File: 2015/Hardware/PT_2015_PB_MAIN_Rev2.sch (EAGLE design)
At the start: 135 parts, among them Q1 Q_ACS711LC, Q11 Q_IRFS7437PbF, Q12 2N7002, Q14 Q_IRFS7437PbF, Q16 Q_IRFS7437PbF, Q18 Q_FDT86102LZ, Q20 Q_IRFS7437PbF, Q4 Q_ACS711LC, Q5 Q_ACS711LC, Q6 Q_IRFS7437PbF, Q7 Q_IRFS7437PbF, Q9 Q_IRFS7437PbF

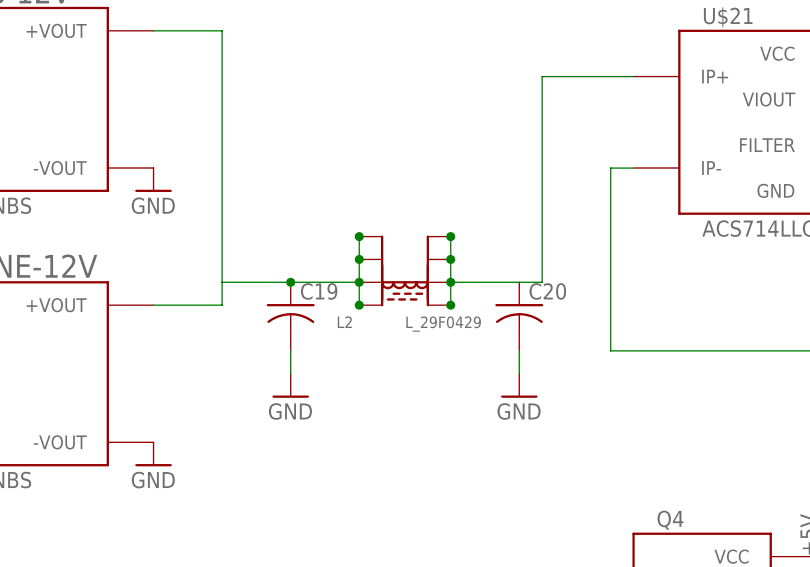
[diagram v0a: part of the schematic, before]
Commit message: Removed ferrite bede on 12V non-critical output
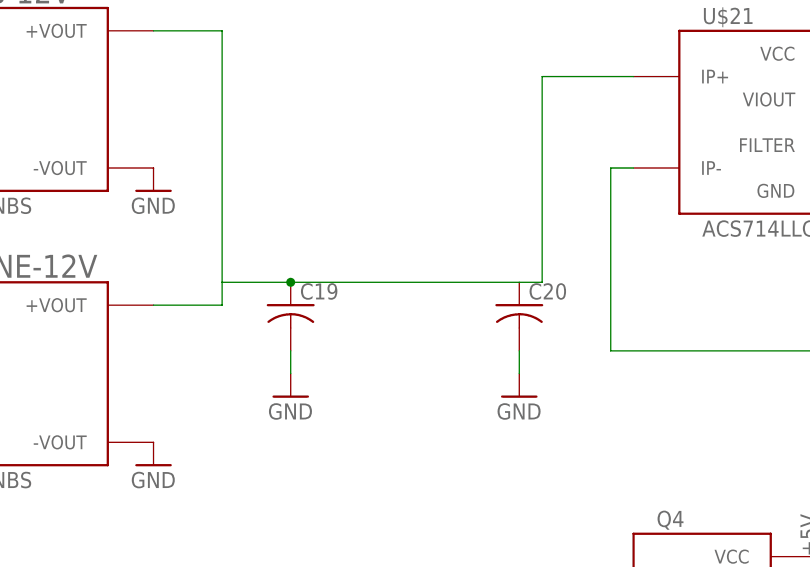
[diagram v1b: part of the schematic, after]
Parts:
- removed L2: L_29F0429, MRDT-2014-All:L_29F0429
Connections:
- removed net N$11: C20.1, L2.5, L2.6, L2.7, L2.8, U$21.IP+
- net N$7: now also C20.1, U$21.IP+; no longer L2.1, L2.2, L2.3, L2.4

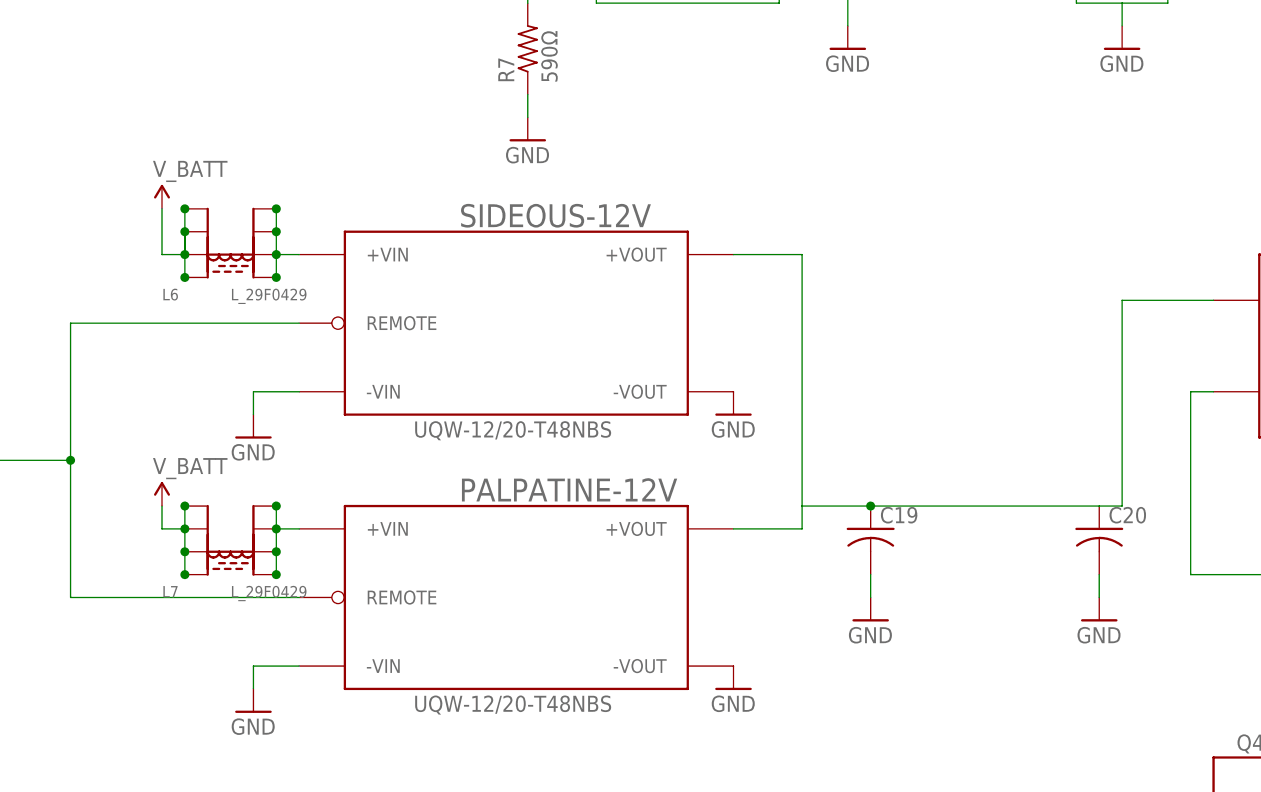
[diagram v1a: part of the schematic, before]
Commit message: Replaced input ferrites and output caps on 12V NC
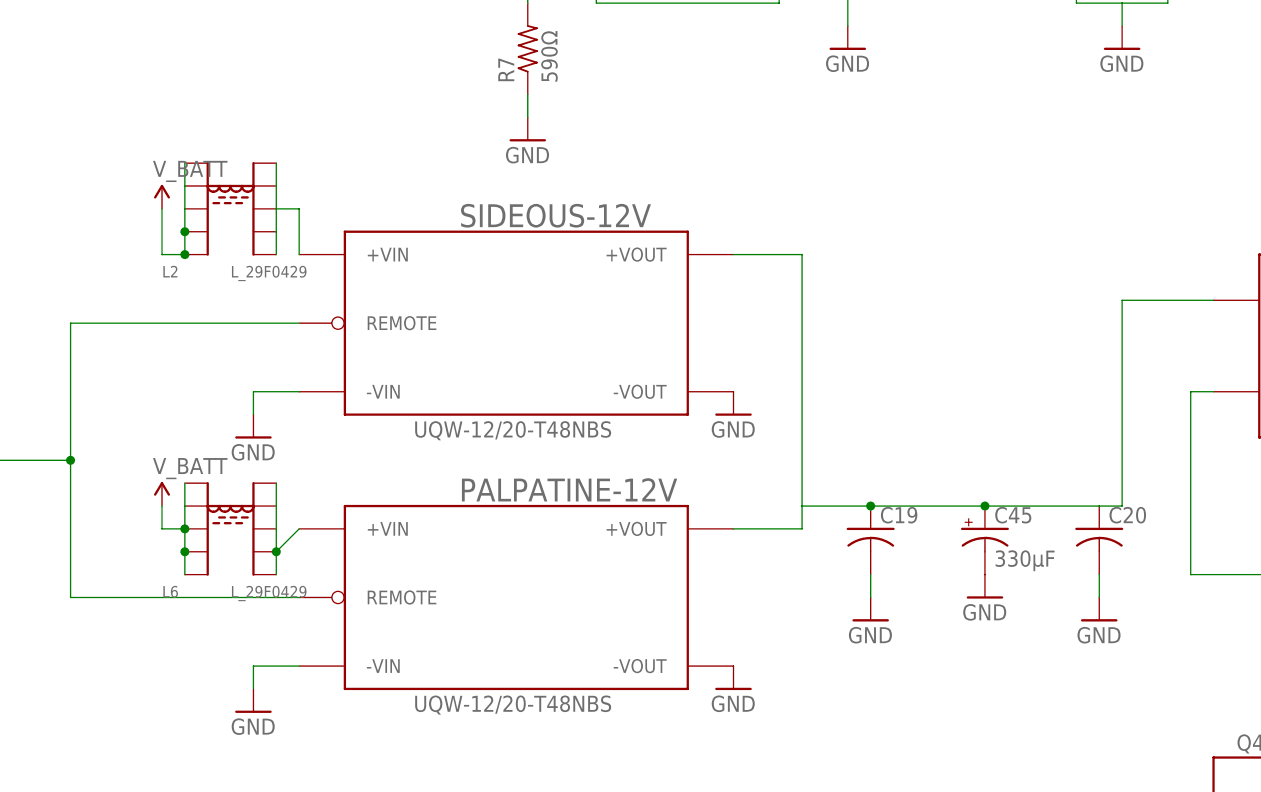
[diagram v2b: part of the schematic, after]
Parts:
- removed L7: L_29F0429, MRDT-2014-All:L_29F0429
- added C45: 330µF, resistor:CPOL-USE5-8.5
- added L2: L_29F0429, MRDT-2015-PowerBoard:L_29F0429
- L6: device MRDT-2014-All:L_29F0429 -> MRDT-2015-PowerBoard:L_29F0429
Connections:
- net GND: now also C45.-
- net N$5: now also L6.10, L6.6, L6.7, L6.8; no longer L7.5, L7.6, L7.7, L7.8
- net N$6: now also L2.10, L2.6, L2.7, L2.8, L2.9; no longer L6.5, L6.6, L6.7, L6.8
- net N$7: now also C45.+
- net V_BATT: now also L2.1, L2.2, L2.3, L2.4, L2.5, L6.5; no longer L7.1, L7.2, L7.3, L7.4
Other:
- moved on the sheet: L6
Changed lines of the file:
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@@
 <?xml version="1.0" encoding="utf-8"?>
 <!DOCTYPE eagle SYSTEM "eagle.dtd">
-<eagle version="7.0.0">
+<eagle version="6.5.0">
 <drawing>
 <settings>
@@
 <part name="L4" library="MRDT-2014-All" deviceset="L_29F0429" device=""/>
 <part name="L5" library="MRDT-2014-All" deviceset="L_29F0429" device=""/>
-<part name="L6" library="MRDT-2014-All" deviceset="L_29F0429" device=""/>
-<part name="L7" library="MRDT-2014-All" deviceset="L_29F0429" device=""/>
 <part name="L8" library="MRDT-2014-All" deviceset="L_29F0429" device=""/>
 <part name="U$2" library="MRDT-2014-All" deviceset="D_SD12T1G" device=""/>
@@
 <part name="GND89" library="SparkFun-Aesthetics" deviceset="GND" device=""/>
 <part name="ARM_P" library="MRDT-2015-PowerBoard" deviceset="H_WR-TBL_32*1*0002" device="HORIZ"/>
+<part name="C45" library="resistor" deviceset="CPOL-US" device="E5-8.5" value="330µF"/>
+<part name="GND90" library="SparkFun-Aesthetics" deviceset="GND" device=""/>
+<part name="L2" library="MRDT-2015-PowerBoard" deviceset="L_29F0429" device=""/>
+<part name="L6" library="MRDT-2015-PowerBoard" deviceset="L_29F0429" device=""/>
 </parts>
 <sheets>
@@
 <instance part="L4" gate="G$1" x="106.68" y="0"/>
 <instance part="L5" gate="G$1" x="25.4" y="119.38"/>
-<instance part="L6" gate="G$1" x="33.02" y="81.28"/>
-<instance part="L7" gate="G$1" x="33.02" y="48.26"/>
 <instance part="L8" gate="G$1" x="25.4" y="-2.54"/>
 <instance part="U$2" gate="G$1" x="129.54" y="-5.08" rot="R90"/>
@@
 <instance part="GND89" gate="1" x="-474.98" y="200.66"/>
 <instance part="ARM_P" gate="G$1" x="-528.32" y="144.78"/>
+<instance part="C45" gate="G$1" x="116.84" y="50.8"/>
+<instance part="GND90" gate="1" x="116.84" y="43.18"/>
+<instance part="L2" gate="G$1" x="33.02" y="83.82"/>
+<instance part="L6" gate="G$1" x="33.02" y="48.26"/>
 </instances>
 <busses>
@@
 <pinref part="C44" gate="G$1" pin="2"/>
 <pinref part="GND89" gate="1" pin="GND"/>
+</segment>
+<segment>
+<pinref part="C45" gate="G$1" pin="-"/>
+<pinref part="GND90" gate="1" pin="GND"/>
 </segment>
 </net>
@@
 <pinref part="SUPPLY3" gate="G$1" pin="V_BATT"/>
 <wire x1="25.4" y1="81.28" x2="25.4" y2="86.36" width="0.1524" layer="91"/>
-<pinref part="L6" gate="G$1" pin="1"/>
 <wire x1="25.4" y1="81.28" x2="27.94" y2="81.28" width="0.1524" layer="91"/>
-<pinref part="L6" gate="G$1" pin="2"/>
-<wire x1="27.94" y1="78.74" x2="27.94" y2="81.28" width="0.1524" layer="91"/>
-<pinref part="L6" gate="G$1" pin="3"/>
-<wire x1="27.94" y1="83.82" x2="27.94" y2="81.28" width="0.1524" layer="91"/>
-<pinref part="L6" gate="G$1" pin="4"/>
+<junction x="27.94" y="81.28"/>
 <wire x1="27.94" y1="81.28" x2="27.94" y2="83.82" width="0.1524" layer="91"/>
-<junction x="27.94" y="78.74"/>
-<junction x="27.94" y="81.28"/>
+<pinref part="L2" gate="G$1" pin="3"/>
+<pinref part="L2" gate="G$1" pin="2"/>
+<wire x1="27.94" y1="83.82" x2="27.94" y2="86.36" width="0.1524" layer="91"/>
 <junction x="27.94" y="83.82"/>
-<wire x1="27.94" y1="83.82" x2="27.94" y2="86.36" width="0.1524" layer="91"/>
-<junction x="27.94" y="86.36"/>
+<pinref part="L2" gate="G$1" pin="1"/>
+<pinref part="L2" gate="G$1" pin="4"/>
+<wire x1="27.94" y1="88.9" x2="27.94" y2="86.36" width="0.1524" layer="91"/>
+<pinref part="L2" gate="G$1" pin="5"/>
+<wire x1="27.94" y1="91.44" x2="27.94" y2="88.9" width="0.1524" layer="91"/>
 </segment>
 <segment>
 <pinref part="SUPPLY4" gate="G$1" pin="V_BATT"/>
 <wire x1="25.4" y1="50.8" x2="25.4" y2="53.34" width="0.1524" layer="91"/>
-<pinref part="L7" gate="G$1" pin="3"/>
 <wire x1="25.4" y1="50.8" x2="27.94" y2="50.8" width="0.1524" layer="91"/>
-<pinref part="L7" gate="G$1" pin="4"/>
 <wire x1="27.94" y1="50.8" x2="27.94" y2="53.34" width="0.1524" layer="91"/>
-<pinref part="L7" gate="G$1" pin="2"/>
+<wire x1="27.94" y1="45.72" x2="27.94" y2="48.26" width="0.1524" layer="91"/>
+<junction x="27.94" y="50.8"/>
+<pinref part="L6" gate="G$1" pin="4"/>
+<pinref part="L6" gate="G$1" pin="3"/>
+<pinref part="L6" gate="G$1" pin="2"/>
 <wire x1="27.94" y1="48.26" x2="27.94" y2="50.8" width="0.1524" layer="91"/>
-<pinref part="L7" gate="G$1" pin="1"/>
-<wire x1="27.94" y1="45.72" x2="27.94" y2="48.26" width="0.1524" layer="91"/>
-<junction x="27.94" y="53.34"/>
-<junction x="27.94" y="50.8"/>
 <junction x="27.94" y="48.26"/>
-<junction x="27.94" y="45.72"/>
+<pinref part="L6" gate="G$1" pin="1"/>
+<pinref part="L6" gate="G$1" pin="5"/>
+<wire x1="27.94" y1="55.88" x2="27.94" y2="53.34" width="0.1524" layer="91"/>
 </segment>
 <segment>
@@
 <net name="N$5" class="0">
 <segment>
-<pinref part="L7" gate="G$1" pin="8"/>
-<pinref part="L7" gate="G$1" pin="5"/>
-<wire x1="38.1" y1="53.34" x2="38.1" y2="50.8" width="0.1524" layer="91"/>
+<wire x1="38.1" y1="50.8" x2="38.1" y2="48.26" width="0.1524" layer="91"/>
 <pinref part="PALPATINE-12V" gate="G$1" pin="+VIN"/>
-<wire x1="38.1" y1="50.8" x2="38.1" y2="48.26" width="0.1524" layer="91"/>
 <wire x1="38.1" y1="48.26" x2="38.1" y2="45.72" width="0.1524" layer="91"/>
-<junction x="38.1" y="45.72"/>
-<pinref part="L7" gate="G$1" pin="6"/>
 <junction x="38.1" y="48.26"/>
-<pinref part="L7" gate="G$1" pin="7"/>
-<junction x="38.1" y="50.8"/>
-<junction x="38.1" y="53.34"/>
-<wire x1="40.64" y1="50.8" x2="38.1" y2="50.8" width="0.1524" layer="91"/>
-</segment>
-</net>
-<net name="N$6" class="0">
-<segment>
+<wire x1="40.64" y1="50.8" x2="38.1" y2="48.26" width="0.1524" layer="91"/>
+<pinref part="L6" gate="G$1" pin="6"/>
+<pinref part="L6" gate="G$1" pin="7"/>
 <pinref part="L6" gate="G$1" pin="8"/>
-<pinref part="L6" gate="G$1" pin="7"/>
-<wire x1="38.1" y1="86.36" x2="38.1" y2="83.82" width="0.1524" layer="91"/>
-<pinref part="L6" gate="G$1" pin="6"/>
-<wire x1="38.1" y1="81.28" x2="38.1" y2="83.82" width="0.1524" layer="91"/>
-<pinref part="L6" gate="G$1" pin="5"/>
-<wire x1="38.1" y1="81.28" x2="38.1" y2="78.74" width="0.1524" layer="91"/>
-<pinref part="SIDEOUS-12V" gate="G$1" pin="+VIN"/>
-<wire x1="40.64" y1="81.28" x2="38.1" y2="81.28" width="0.1524" layer="91"/>
-<junction x="38.1" y="83.82"/>
-<junction x="38.1" y="86.36"/>
-<junction x="38.1" y="81.28"/>
-<junction x="38.1" y="78.74"/>
+<pinref part="L6" gate="G$1" pin="10"/>
+<wire x1="38.1" y1="55.88" x2="38.1" y2="50.8" width="0.1524" layer="91"/>
 </segment>
 </net>
@@
 <wire x1="142.24" y1="76.2" x2="132.08" y2="76.2" width="0.1524" layer="91"/>
 <wire x1="132.08" y1="76.2" x2="132.08" y2="53.34" width="0.1524" layer="91"/>
-<wire x1="104.14" y1="53.34" x2="129.54" y2="53.34" width="0.1524" layer="91"/>
+<wire x1="104.14" y1="53.34" x2="116.84" y2="53.34" width="0.1524" layer="91"/>
+<pinref part="C45" gate="G$1" pin="+"/>
+<wire x1="116.84" y1="53.34" x2="129.54" y2="53.34" width="0.1524" layer="91"/>
+<junction x="116.84" y="53.34"/>
 </segment>
 </net>
@@
 </segment>
 </net>
+<net name="N$6" class="0">
+<segment>
+<pinref part="L2" gate="G$1" pin="10"/>
+<pinref part="L2" gate="G$1" pin="9"/>
+<wire x1="38.1" y1="91.44" x2="38.1" y2="88.9" width="0.1524" layer="91"/>
+<pinref part="L2" gate="G$1" pin="7"/>
+<pinref part="L2" gate="G$1" pin="8"/>
+<wire x1="38.1" y1="86.36" x2="38.1" y2="83.82" width="0.1524" layer="91"/>
+<wire x1="38.1" y1="81.28" x2="38.1" y2="83.82" width="0.1524" layer="91"/>
+<pinref part="L2" gate="G$1" pin="6"/>
+<wire x1="38.1" y1="88.9" x2="38.1" y2="86.36" width="0.1524" layer="91"/>
+<pinref part="SIDEOUS-12V" gate="G$1" pin="+VIN"/>
+<wire x1="38.1" y1="86.36" x2="40.64" y2="86.36" width="0.1524" layer="91"/>
+<wire x1="40.64" y1="86.36" x2="40.64" y2="81.28" width="0.1524" layer="91"/>
+</segment>
+</net>

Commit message: Added TVS diodes and minor trace adjustments
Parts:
- added D1, D2: 1.5KE36A, diode:15KEXX
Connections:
- net GND: now also D1.A, D2.A
- net V_BATT: now also D1.C, D2.C
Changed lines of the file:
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@@
 <part name="L2" library="MRDT-2015-PowerBoard" deviceset="L_29F0429" device=""/>
 <part name="L6" library="MRDT-2015-PowerBoard" deviceset="L_29F0429" device=""/>
+<part name="D1" library="diode" deviceset="15KEXX" device="" value="1.5KE36A"/>
+<part name="D2" library="diode" deviceset="15KEXX" device="" value="1.5KE36A"/>
 </parts>
 <sheets>
@@
 <instance part="L2" gate="G$1" x="33.02" y="83.82"/>
 <instance part="L6" gate="G$1" x="33.02" y="48.26"/>
+<instance part="D1" gate="1" x="86.36" y="175.26" rot="R90"/>
+<instance part="D2" gate="1" x="78.74" y="175.26" rot="R90"/>
 </instances>
 <busses>
@@
 <pinref part="C1" gate="G$1" pin="-"/>
 <wire x1="96.52" y1="170.18" x2="96.52" y2="167.64" width="0.1524" layer="91"/>
+<pinref part="D2" gate="1" pin="A"/>
+<wire x1="78.74" y1="172.72" x2="78.74" y2="170.18" width="0.1524" layer="91"/>
+<wire x1="78.74" y1="170.18" x2="86.36" y2="170.18" width="0.1524" layer="91"/>
+<wire x1="86.36" y1="170.18" x2="86.36" y2="167.64" width="0.1524" layer="91"/>
+<pinref part="D1" gate="1" pin="A"/>
+<wire x1="86.36" y1="172.72" x2="86.36" y2="170.18" width="0.1524" layer="91"/>
 </segment>
 <segment>
@@
 <pinref part="C4" gate="G$1" pin="+"/>
 <wire x1="127" y1="177.8" x2="127" y2="180.34" width="0.1524" layer="91"/>
-</segment>
-<segment>
+<pinref part="D1" gate="1" pin="C"/>
+<wire x1="86.36" y1="180.34" x2="86.36" y2="177.8" width="0.1524" layer="91"/>
+<pinref part="D2" gate="1" pin="C"/>
+<wire x1="86.36" y1="177.8" x2="78.74" y2="177.8" width="0.1524" layer="91"/>
+</segment>
+<segment>

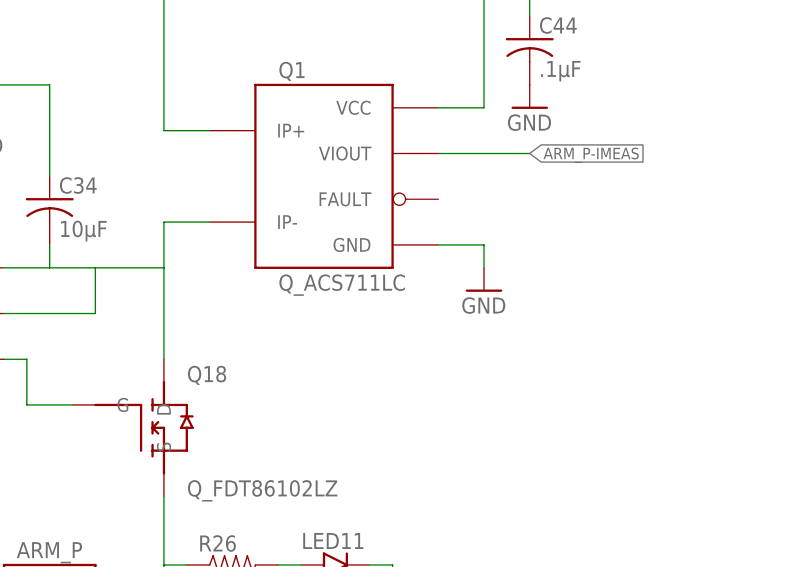
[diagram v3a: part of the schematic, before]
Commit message: Fixed DRC Errors for 3oz Copper
Brought board to spec for 4PCB's 3oz Copper
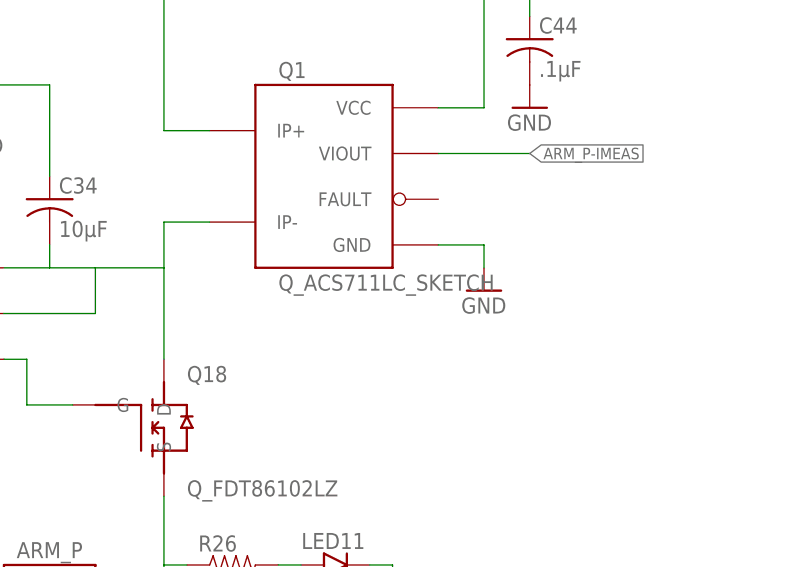
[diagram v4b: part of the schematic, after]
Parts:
- Q1: value Q_ACS711LC -> Q_ACS711LC_SKETCH; device MRDT-2015-PowerBoard:Q_ACS711LC -> MRDT-2015-PowerBoard:Q_ACS711LC_SKETCH
- U$14, U$15, U$16, U$17, U$18, U$19, U$20: device MRDT-2015-PowerBoard:Q_ACS714 -> MRDT-2015-PowerBoard:Q_ACS714_SKETCH
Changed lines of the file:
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@@
 <part name="R28" library="SparkFun-Passives" deviceset="RESISTOR" device="1206" value="1kΩ"/>
 <part name="GND80" library="SparkFun-Aesthetics" deviceset="GND" device=""/>
-<part name="U$14" library="MRDT-2015-PowerBoard" deviceset="Q_ACS714" device="" value="ACS714LLCTR-50A-T"/>
+<part name="U$14" library="MRDT-2015-PowerBoard" deviceset="Q_ACS714" device="_SKETCH" value="ACS714LLCTR-50A-T"/>
 <part name="C37" library="resistor" deviceset="C-US" device="C0805" value="1nF"/>
 <part name="GND81" library="SparkFun-Aesthetics" deviceset="GND" device=""/>
@@
 <part name="P+11" library="supply1" deviceset="+5V" device=""/>
 <part name="P+12" library="supply1" deviceset="+5V" device=""/>
-<part name="U$15" library="MRDT-2015-PowerBoard" deviceset="Q_ACS714" device="" value="ACS714LLCTR-50A-T"/>
+<part name="U$15" library="MRDT-2015-PowerBoard" deviceset="Q_ACS714" device="_SKETCH" value="ACS714LLCTR-50A-T"/>
 <part name="C38" library="resistor" deviceset="C-US" device="C0805" value="1nF"/>
 <part name="GND82" library="SparkFun-Aesthetics" deviceset="GND" device=""/>
@@
 <part name="P+13" library="supply1" deviceset="+5V" device=""/>
 <part name="P+14" library="supply1" deviceset="+5V" device=""/>
-<part name="U$16" library="MRDT-2015-PowerBoard" deviceset="Q_ACS714" device="" value="ACS714LLCTR-50A-T"/>
+<part name="U$16" library="MRDT-2015-PowerBoard" deviceset="Q_ACS714" device="_SKETCH" value="ACS714LLCTR-50A-T"/>
 <part name="C27" library="resistor" deviceset="C-US" device="C0805" value="1nF"/>
 <part name="GND56" library="SparkFun-Aesthetics" deviceset="GND" device=""/>
@@
 <part name="P+15" library="supply1" deviceset="+5V" device=""/>
 <part name="P+16" library="supply1" deviceset="+5V" device=""/>
-<part name="U$17" library="MRDT-2015-PowerBoard" deviceset="Q_ACS714" device="" value="ACS714LLCTR-50A-T"/>
+<part name="U$17" library="MRDT-2015-PowerBoard" deviceset="Q_ACS714" device="_SKETCH" value="ACS714LLCTR-50A-T"/>
 <part name="C31" library="resistor" deviceset="C-US" device="C0805" value="1nF"/>
 <part name="GND66" library="SparkFun-Aesthetics" deviceset="GND" device=""/>
@@
 <part name="P+17" library="supply1" deviceset="+5V" device=""/>
 <part name="P+18" library="supply1" deviceset="+5V" device=""/>
-<part name="U$18" library="MRDT-2015-PowerBoard" deviceset="Q_ACS714" device="" value="ACS714LLCTR-50A-T"/>
+<part name="U$18" library="MRDT-2015-PowerBoard" deviceset="Q_ACS714" device="_SKETCH" value="ACS714LLCTR-50A-T"/>
 <part name="C35" library="resistor" deviceset="C-US" device="C0805" value="1nF"/>
 <part name="GND76" library="SparkFun-Aesthetics" deviceset="GND" device=""/>
@@
 <part name="P+19" library="supply1" deviceset="+5V" device=""/>
 <part name="P+20" library="supply1" deviceset="+5V" device=""/>
-<part name="U$19" library="MRDT-2015-PowerBoard" deviceset="Q_ACS714" device="" value="ACS714LLCTR-50A-T"/>
+<part name="U$19" library="MRDT-2015-PowerBoard" deviceset="Q_ACS714" device="_SKETCH" value="ACS714LLCTR-50A-T"/>
 <part name="C40" library="resistor" deviceset="C-US" device="C0805" value="1nF"/>
 <part name="GND84" library="SparkFun-Aesthetics" deviceset="GND" device=""/>
@@
 <part name="P+21" library="supply1" deviceset="+5V" device=""/>
 <part name="P+22" library="supply1" deviceset="+5V" device=""/>
-<part name="U$20" library="MRDT-2015-PowerBoard" deviceset="Q_ACS714" device="" value="ACS714LLCTR-50A-T"/>
+<part name="U$20" library="MRDT-2015-PowerBoard" deviceset="Q_ACS714" device="_SKETCH" value="ACS714LLCTR-50A-T"/>
 <part name="C42" library="resistor" deviceset="C-US" device="C0805" value="1nF"/>
 <part name="GND86" library="SparkFun-Aesthetics" deviceset="GND" device=""/>
@@
 <part name="C43" library="resistor" deviceset="C-US" device="C0805" value="1nF"/>
 <part name="GND87" library="SparkFun-Aesthetics" deviceset="GND" device=""/>
-<part name="Q1" library="MRDT-2015-PowerBoard" deviceset="Q_ACS711*LC" device=""/>
+<part name="Q1" library="MRDT-2015-PowerBoard" deviceset="Q_ACS711*LC" device="_SKETCH" value="Q_ACS711LC_SKETCH"/>
 <part name="GND88" library="SparkFun-Aesthetics" deviceset="GND" device=""/>
 <part name="P+24" library="supply1" deviceset="+5V" device=""/>
